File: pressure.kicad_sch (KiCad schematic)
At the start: 12 parts, among them U5 TLV9101IDBVR

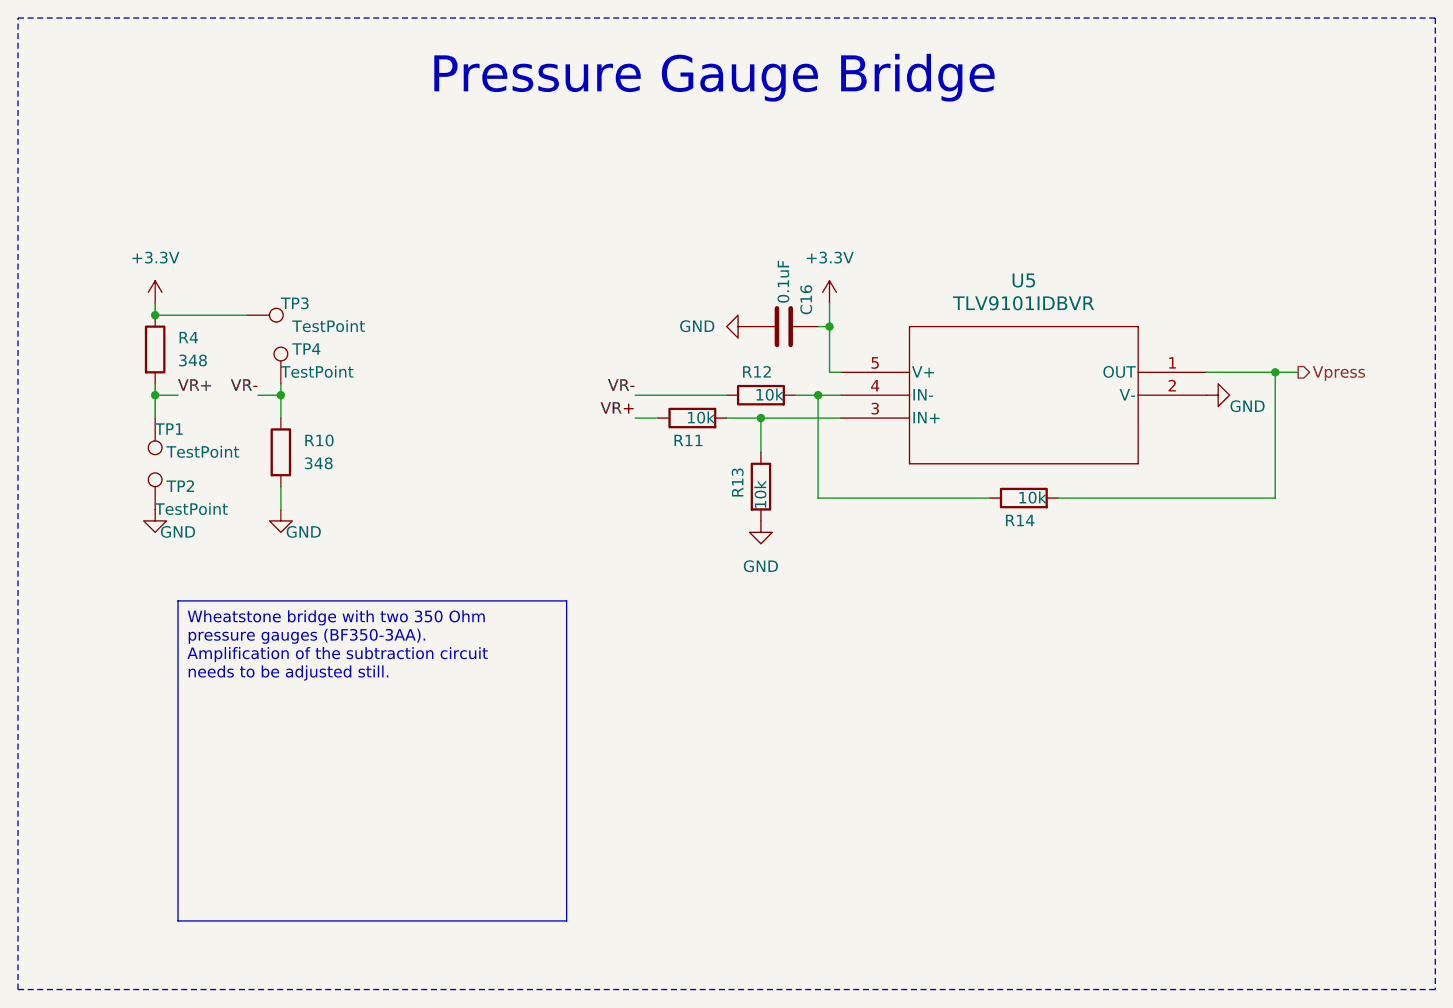
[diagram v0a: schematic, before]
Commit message: remove ATTiny; fix LED footprints; start cleanup
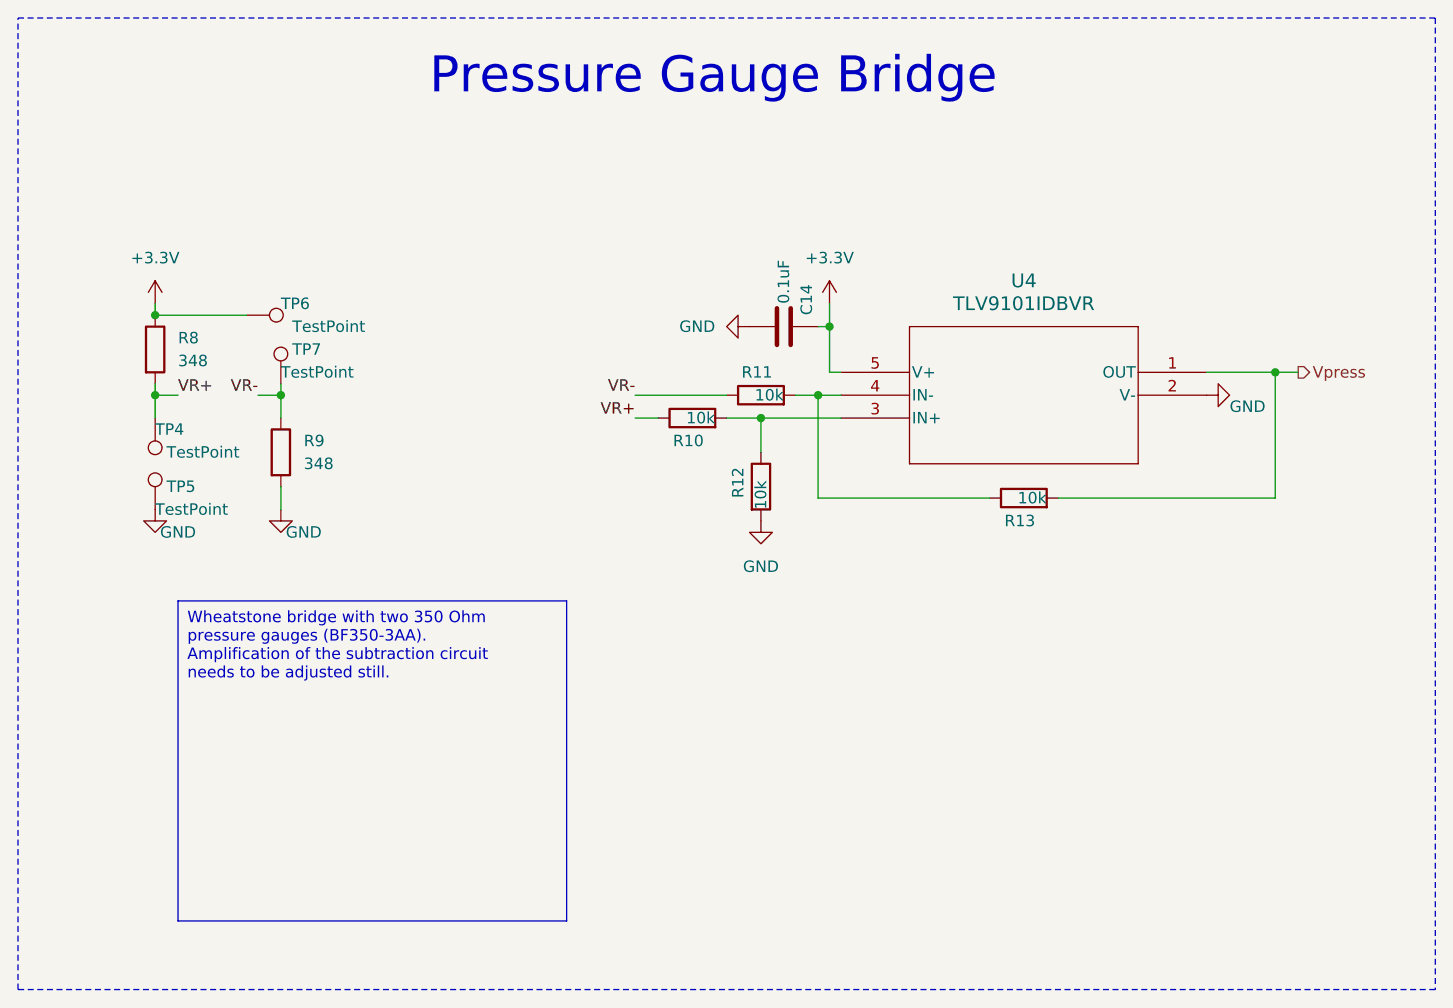
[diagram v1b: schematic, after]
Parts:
- renumbered C16 to C14, R11 to R10, R12 to R11, R13 to R12, R14 to R13, R4 to R8, R10 to R9, TP1 to TP4, TP2 to TP5, TP3 to TP6, TP4 to TP7, U5 to U4

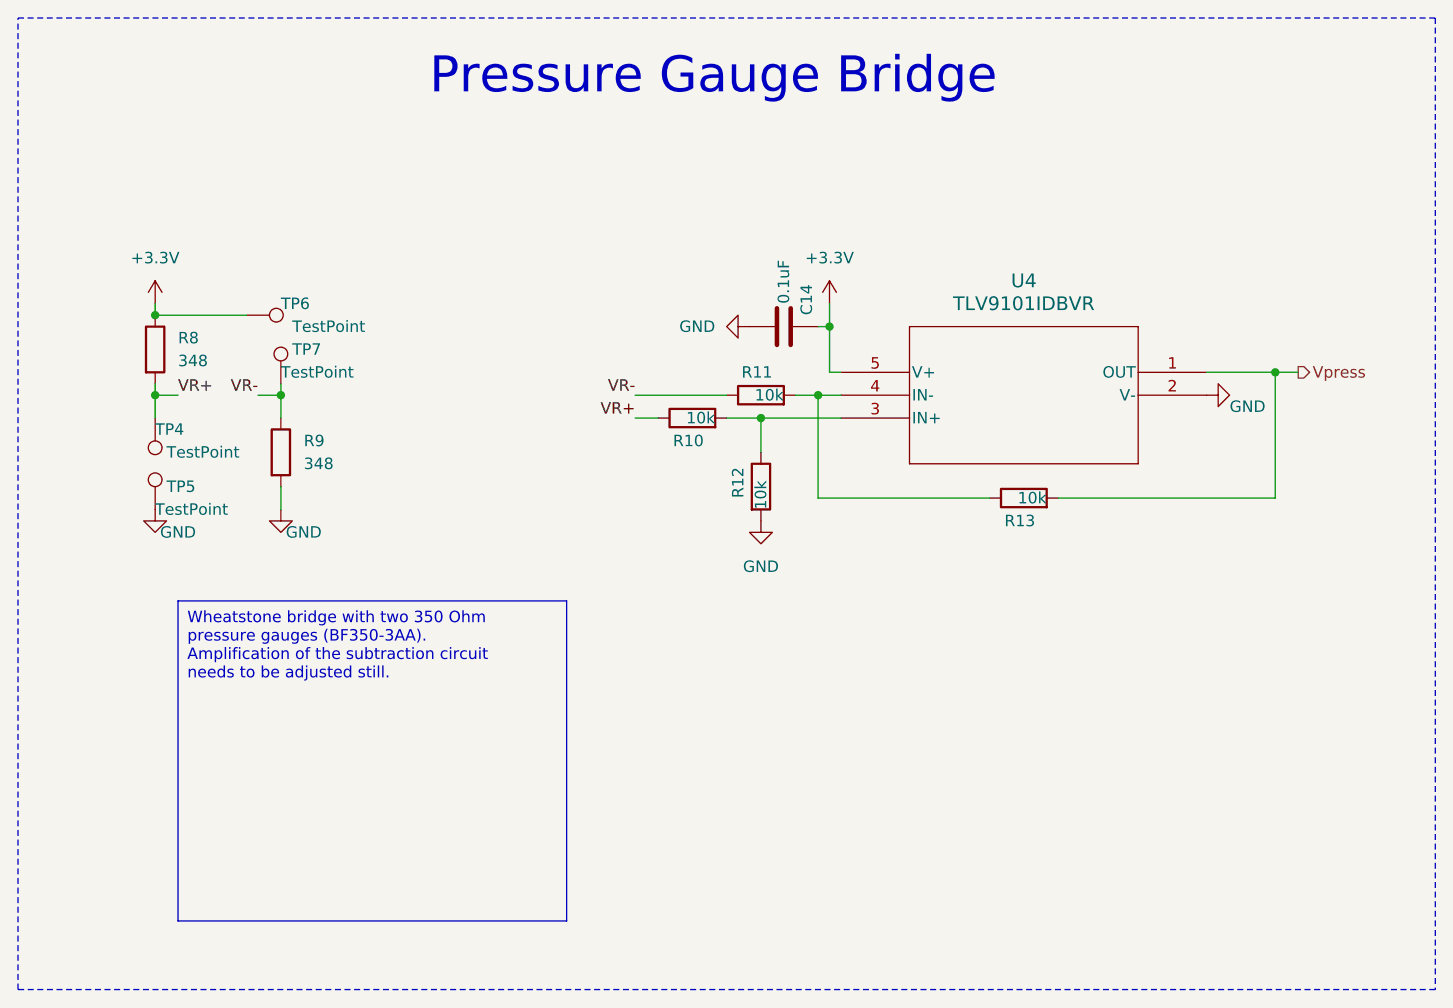
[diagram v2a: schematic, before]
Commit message: change pressure bridge to four DMS
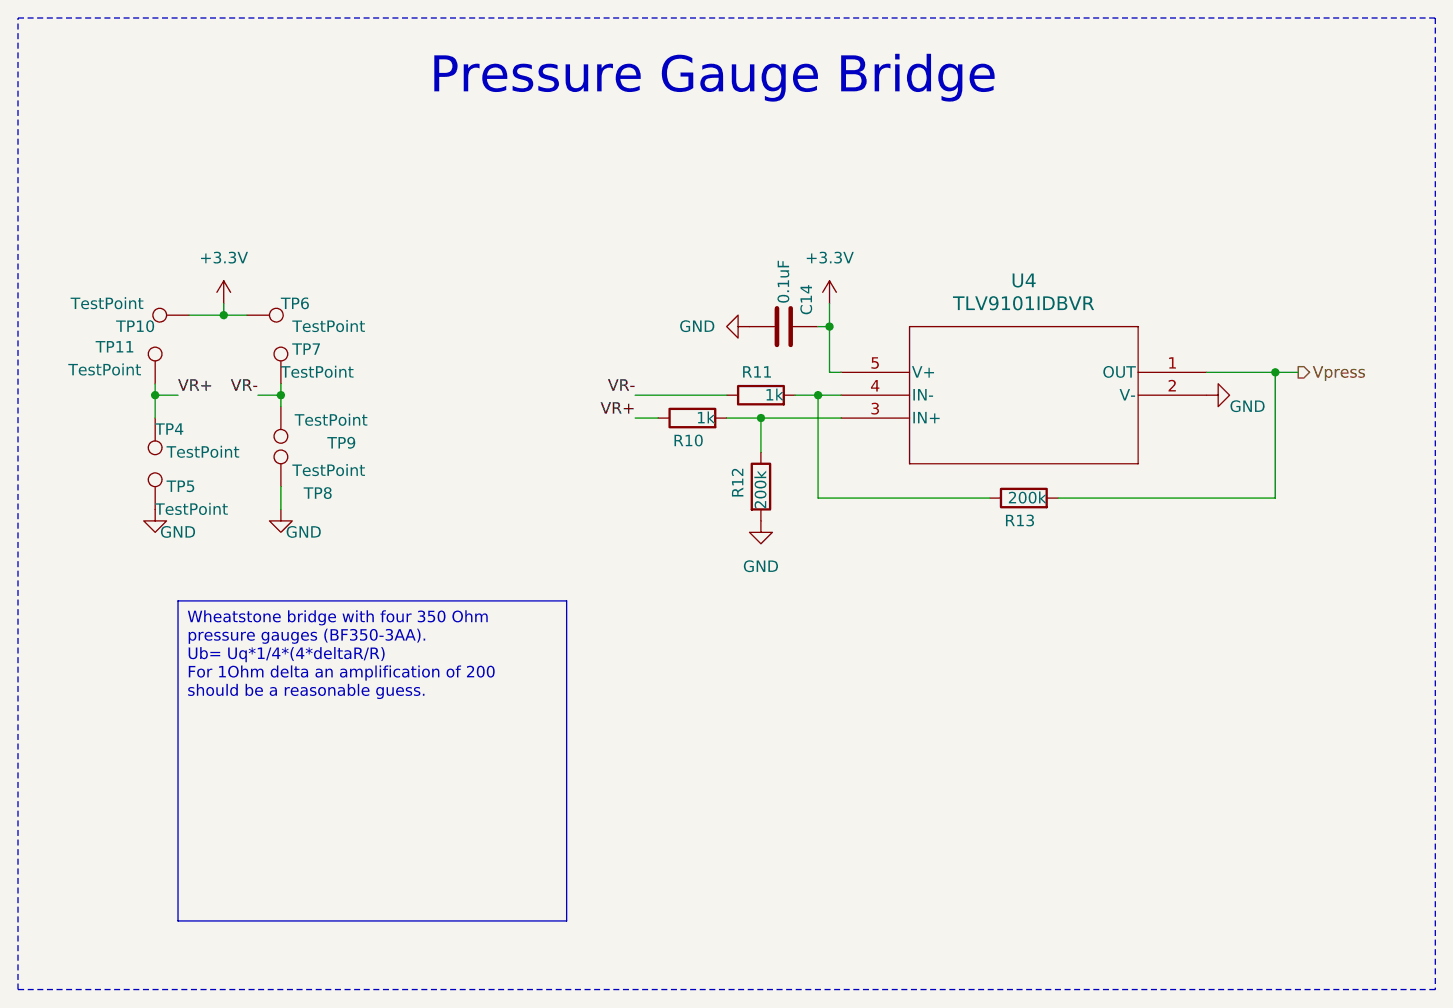
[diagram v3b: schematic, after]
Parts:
- removed R8, R9: 348, Resistor_SMD:R_0805_2012Metric, symbol Device:R
- added TP10, TP11, TP8, TP9: TestPoint, TestPoint:TestPoint_Pad_D2.0mm, symbol Connector:TestPoint
- R10, R11: value 10k -> 1k
- R12, R13: value 10k -> 200k
- TP4, TP5, TP6, TP7: footprint TestPoint:TestPoint_Pad_D3.0mm -> TestPoint:TestPoint_Pad_D2.0mm
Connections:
- net +3.3V: now also TP10.1
- net GND: now also TP8.1
- net VR+: now also TP11.1
- net VR-: now also TP9.1

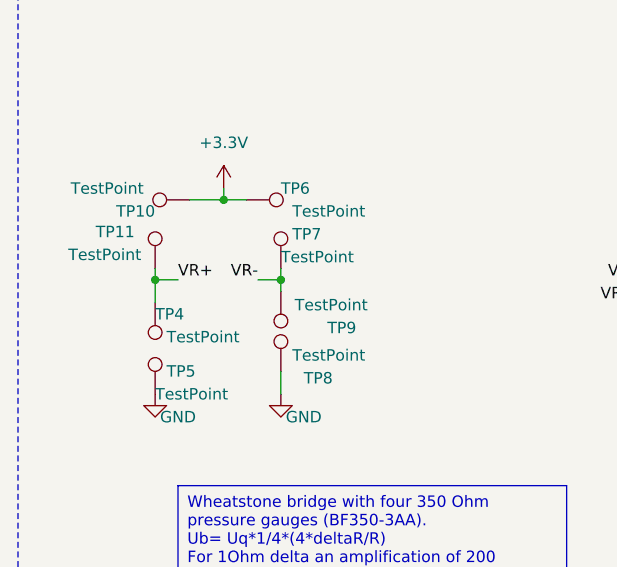
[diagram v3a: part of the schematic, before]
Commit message: change to 2 pressure gauge strips
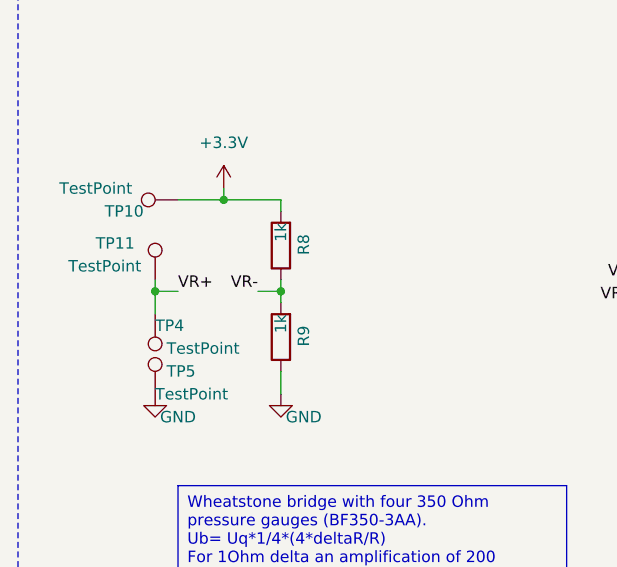
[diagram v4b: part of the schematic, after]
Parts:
- removed TP6, TP7, TP8, TP9: TestPoint, TestPoint:TestPoint_Pad_D2.0mm, symbol Connector:TestPoint
- added R8, R9: 1k, Resistor_SMD:R_0805_2012Metric, symbol Device:R
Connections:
- net +3.3V: now also R8.2
- net GND: now also R9.1
- net VR-: now also R8.1, R9.2
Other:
- moved on the sheet: TP10, TP11, TP4

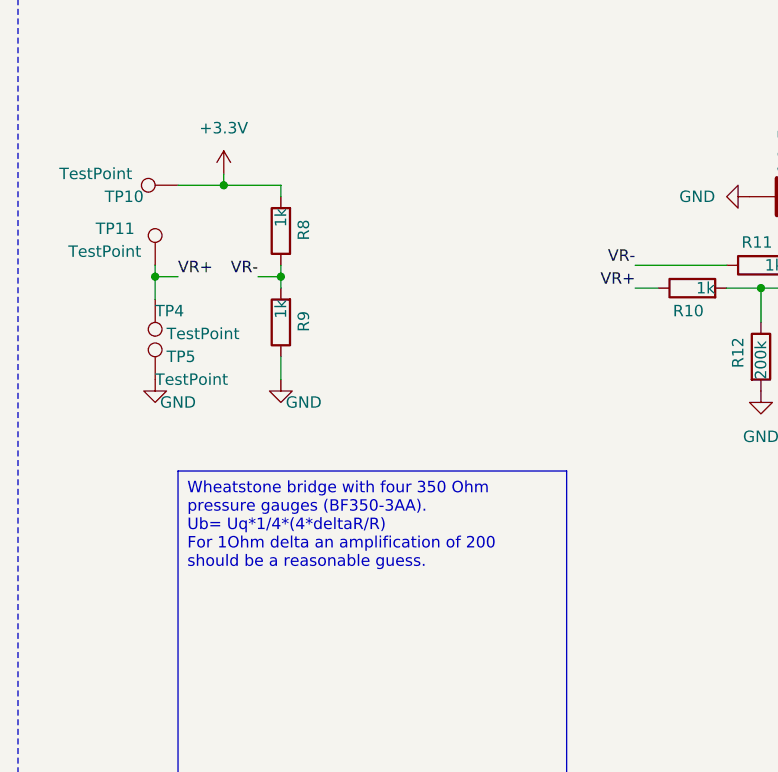
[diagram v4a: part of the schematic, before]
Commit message: update design; add 3d models to everything; add notches to PCB
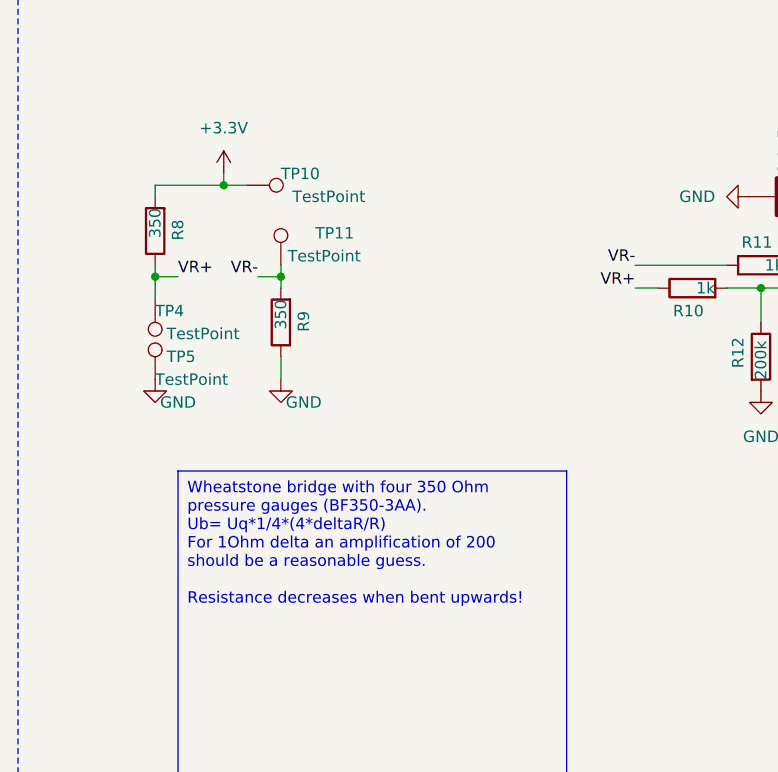
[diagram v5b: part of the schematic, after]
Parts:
- R8, R9: value 1k -> 350
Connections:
- net VR+: now also R8.1; no longer TP11.1
- net VR-: now also TP11.1; no longer R8.1
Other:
- moved on the sheet: R8, TP10, TP11
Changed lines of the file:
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@@
 	(wire
 		(pts
-			(xy 48.26 53.34) (xy 54.61 53.34)
+			(xy 48.26 53.34) (xy 50.8 53.34)
 		)
 		(stroke
@@
 	(wire
 		(pts
-			(xy 54.61 53.34) (xy 54.61 54.61)
-		)
-		(stroke
-			(width 0)
-			(type default)
-		)
-	)
-	(wire
-		(pts
 			(xy 133.35 73.66) (xy 114.3 73.66)
 		)
@@
 	(wire
 		(pts
+			(xy 40.64 53.34) (xy 48.26 53.34)
+		)
+		(stroke
+			(width 0)
+			(type default)
+		)
+	)
+	(wire
+		(pts
 			(xy 40.64 66.04) (xy 40.64 63.5)
 		)
@@
 	(wire
 		(pts
-			(xy 43.18 53.34) (xy 48.26 53.34)
+			(xy 40.64 53.34) (xy 40.64 54.61)
 		)
 		(stroke
@@
 		)
 	)
-	(text_box "Wheatstone bridge with four 350 Ohm pressure gauges (BF350-3AA).\nUb= Uq*1/4*(4*deltaR/R)\nFor 1Ohm delta an amplification of 200 should be a reasonable guess."
+	(text_box "Wheatstone bridge with four 350 Ohm pressure gauges (BF350-3AA).\nUb= Uq*1/4*(4*deltaR/R)\nFor 1Ohm delta an amplification of 200 should be a reasonable guess.\n\nResistance decreases when bent upwards!"
 		(exclude_from_sim no)
 		(at 43.18 85.09 0)
@@
 	(symbol
 		(lib_id "Connector:TestPoint")
-		(at 40.64 62.23 0)
+		(at 54.61 62.23 0)
 		(unit 1)
 		(exclude_from_sim no)
@@
 		(dnp no)
 		(property "Reference" "TP11"
-			(at 34.036 58.166 0)
+			(at 58.42 58.674 0)
 			(effects
 				(font
@@
 		)
 		(property "Value" "TestPoint"
-			(at 30.988 60.706 0)
+			(at 55.372 61.214 0)
 			(effects
 				(font
@@
 		)
 		(property "Footprint" "TestPoint:TestPoint_Pad_D2.0mm"
-			(at 45.72 62.23 0)
+			(at 59.69 62.23 0)
 			(effects
 				(font
@@
 		)
 		(property "Datasheet" "~"
-			(at 45.72 62.23 0)
+			(at 59.69 62.23 0)
 			(effects
 				(font
@@
 		)
 		(property "Description" "test point"
-			(at 40.64 62.23 0)
+			(at 54.61 62.23 0)
 			(effects
 				(font
@@
 		)
 		(property "mpn" ""
-			(at 40.64 62.23 0)
+			(at 54.61 62.23 0)
 			(effects
 				(font
@@
 	(symbol
 		(lib_id "Connector:TestPoint")
-		(at 43.18 53.34 90)
+		(at 50.8 53.34 270)
 		(unit 1)
 		(exclude_from_sim no)
@@
 		(dnp no)
 		(property "Reference" "TP10"
-			(at 39.37 54.61 90)
+			(at 54.61 52.07 90)
 			(effects
 				(font
@@
 		)
 		(property "Value" "TestPoint"
-			(at 38.1 52.07 90)
+			(at 55.88 54.61 90)
 			(effects
 				(font
@@
 		)
 		(property "Footprint" "TestPoint:TestPoint_Pad_D2.0mm"
-			(at 43.18 48.26 0)
+			(at 50.8 58.42 0)
 			(effects
 				(font
@@
 		)
 		(property "Datasheet" "~"
-			(at 43.18 48.26 0)
+			(at 50.8 58.42 0)
 			(effects
 				(font
@@
 		)
 		(property "Description" "test point"
-			(at 43.18 53.34 0)
+			(at 50.8 53.34 0)
 			(effects
 				(font
@@
 		)
 		(property "mpn" ""
-			(at 43.18 53.34 0)
+			(at 50.8 53.34 0)
 			(effects
 				(font
@@
 	(symbol
 		(lib_id "Device:R")
-		(at 54.61 58.42 180)
+		(at 40.64 58.42 180)
 		(unit 1)
 		(exclude_from_sim no)
@@
 		(dnp no)
 		(property "Reference" "R8"
-			(at 57.15 57.15 90)
-			(effects
-				(font
-					(size 1.27 1.27)
-				)
-				(justify left)
-			)
-		)
-		(property "Value" "1k"
-			(at 54.61 55.88 90)
+			(at 43.18 57.15 90)
+			(effects
+				(font
+					(size 1.27 1.27)
+				)
+				(justify left)
+			)
+		)
+		(property "Value" "350"
+			(at 40.64 55.88 90)
 			(effects
 				(font
@@
 		)
 		(property "Footprint" "Resistor_SMD:R_0805_2012Metric"
-			(at 56.388 58.42 90)
+			(at 42.418 58.42 90)
 			(effects
 				(font
@@
 		)
 		(property "Datasheet" "~"
-			(at 54.61 58.42 0)
+			(at 40.64 58.42 0)
 			(effects
 				(font
@@
 		)
 		(property "Description" "Resistor"
-			(at 54.61 58.42 0)
+			(at 40.64 58.42 0)
 			(effects
 				(font
@@
 		)
 		(property "mpn" "CR0805-FX-1002ELF "
-			(at 54.61 58.42 0)
+			(at 40.64 58.42 0)
 			(effects
 				(font
@@
 			)
 		)
-		(property "Value" "1k"
+		(property "Value" "350"
 			(at 54.61 66.04 90)
 			(effects
